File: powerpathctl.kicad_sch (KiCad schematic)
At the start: 10 parts, among them J10 Conn_01x06_Male, J11 Conn_01x06_Male_BAT_data, J8 Conn_01x03_Male_BAT_PWR_IN_NU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, J9 Conn_01x03_Male_BAT_PWR, Q1 SI7149ADP-T1-GE3, U7 LTC4412ES6

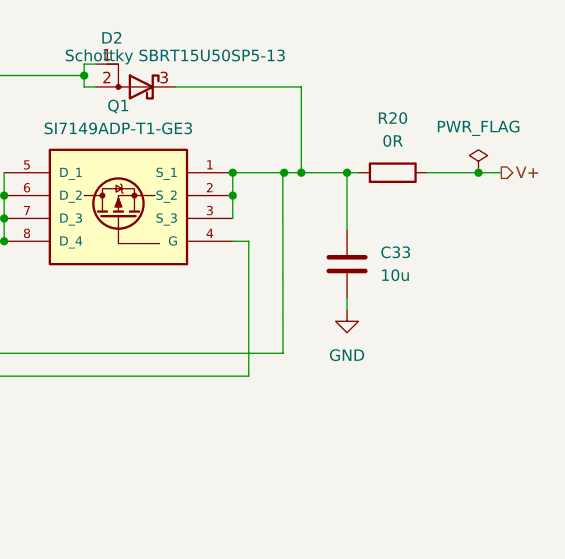
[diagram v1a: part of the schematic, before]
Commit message: optimized component selection, assigned missing LCSC part numbers
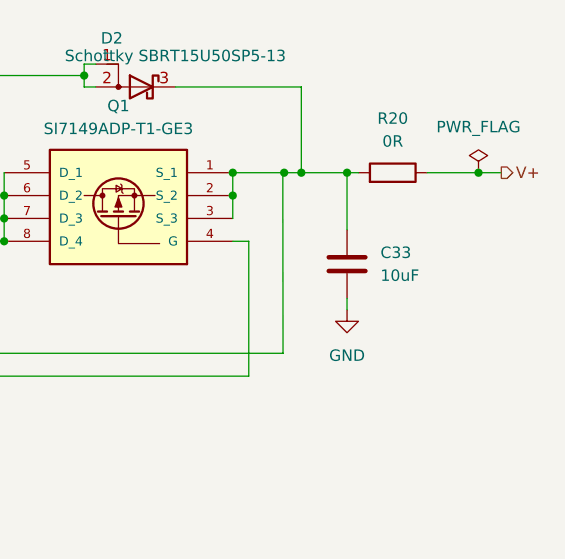
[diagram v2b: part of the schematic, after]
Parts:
- C33: value 10u -> 10uF
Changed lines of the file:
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@@
       (effects (font (size 1.27 1.27)) (justify left))
     )
-    (property "Value" "10u" (id 1) (at 192.9384 78.7399 0)
+    (property "Value" "10uF" (id 1) (at 192.9384 78.7399 0)
       (effects (font (size 1.27 1.27)) (justify left))
     )

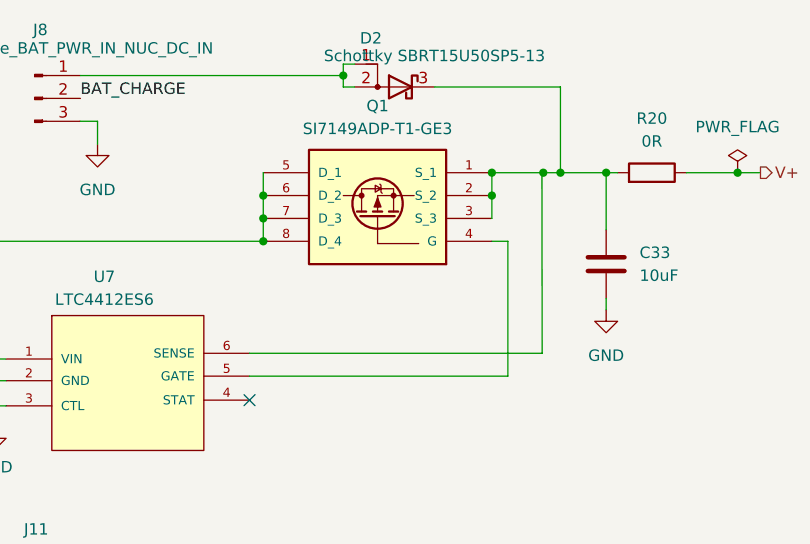
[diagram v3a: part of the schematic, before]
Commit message: motor connectors, optimized power path controller layout
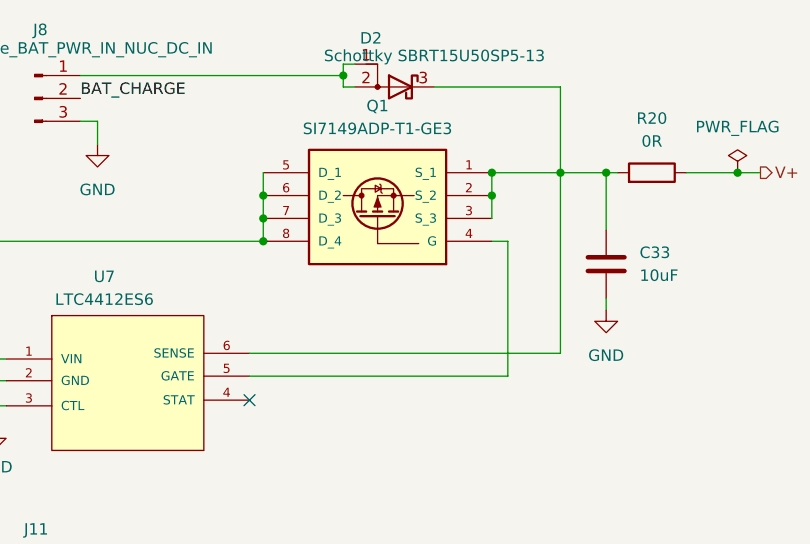
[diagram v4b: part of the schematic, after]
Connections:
- net at C33.1, D2.3 (K), R20.2: now also Q1.1 (S_1), Q1.2 (S_2), Q1.3 (S_3), U7.6 (SENSE)
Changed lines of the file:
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@@
   (junction (at 111.3028 120.269) (diameter 0) (color 0 0 0 0)
   )
-  (junction (at 184.15 67.31) (diameter 0) (color 0 0 0 0)
+  (junction (at 176.53 67.31) (diameter 0) (color 0 0 0 0)
   )
   (junction (at 151.13 69.85) (diameter 0) (color 0 0 0 0)
@@
   )
   (junction (at 121.285 74.93) (diameter 0) (color 0 0 0 0)
-  )
-  (junction (at 176.53 67.31) (diameter 0) (color 0 0 0 0)
   )
   (junction (at 151.13 74.93) (diameter 0) (color 0 0 0 0)
@@
   (junction (at 92.71 80.01) (diameter 0) (color 0 0 0 0)
   )
-  (junction (at 182.245 67.31) (diameter 0) (color 0 0 0 0)
+  (junction (at 151.13 72.39) (diameter 0) (color 0 0 0 0)
   )
-  (junction (at 151.13 72.39) (diameter 0) (color 0 0 0 0)
+  (junction (at 184.15 67.31) (diameter 0) (color 0 0 0 0)
   )
   (no_connect (at 149.606 92.583))
   (wire (pts (xy 132.715 61.595) (xy 132.715 64.135))
+    (stroke (width 0) (type default) (color 0 0 0 0))
+  )
+  (wire (pts (xy 176.53 67.31) (xy 184.15 67.31))
     (stroke (width 0) (type default) (color 0 0 0 0))
   )
@@
     (stroke (width 0) (type default) (color 0 0 0 0))
   )
+  (wire (pts (xy 184.15 87.376) (xy 184.15 67.31))
+    (stroke (width 0) (type default) (color 0 0 0 0))
+  )
   (wire (pts (xy 189.23 67.31) (xy 189.23 73.66))
     (stroke (width 0) (type default) (color 0 0 0 0))
@@
     (stroke (width 0) (type default) (color 0 0 0 0))
   )
+  (wire (pts (xy 149.606 87.376) (xy 184.15 87.376))
+    (stroke (width 0) (type default) (color 0 0 0 0))
+  )
   (wire (pts (xy 176.53 69.85) (xy 176.53 72.39))
     (stroke (width 0) (type default) (color 0 0 0 0))
   )
   (wire (pts (xy 108.6104 125.349) (xy 122.6312 125.349))
-    (stroke (width 0) (type default) (color 0 0 0 0))
-  )
-  (wire (pts (xy 182.245 67.31) (xy 184.15 67.31))
     (stroke (width 0) (type default) (color 0 0 0 0))
   )
@@
     (stroke (width 0) (type default) (color 0 0 0 0))
   )
-  (wire (pts (xy 149.606 87.376) (xy 182.118 87.376))
-    (stroke (width 0) (type default) (color 0 0 0 0))
-  )
   (wire (pts (xy 170.18 57.785) (xy 184.15 57.785))
     (stroke (width 0) (type default) (color 0 0 0 0))
   )
-  (wire (pts (xy 182.118 87.376) (xy 182.0926 67.31))
-    (stroke (width 0) (type default) (color 0 0 0 0))
-  )
-  (wire (pts (xy 176.53 67.31) (xy 182.0926 67.31))
-    (stroke (width 0) (type default) (color 0 0 0 0))
-  )

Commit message: more routing and pinout opt
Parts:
- removed R20, R21: 0R, Resistor_SMD:R_0603_1608Metric, symbol Device:R
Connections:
- net V+: now also C33.1, D2.3 (K), Q1.1 (S_1), Q1.2 (S_2), Q1.3 (S_3), U7.6 (SENSE)
- net VBAT+: now also Q1.5 (D_1), Q1.6 (D_2), Q1.7 (D_3), Q1.8 (D_4), U7.1 (VIN)
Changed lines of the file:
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@@
-    (stroke (width 0) (type default) (color 0 0 0 0))
-  )
-  (wire (pts (xy 120.015 74.93) (xy 121.285 74.93))
-    (stroke (width 0) (type default) (color 0 0 0 0))
-  )
-  (wire (pts (xy 198.12 67.31) (xy 203.835 67.31))
     (stroke (width 0) (type default) (color 0 0 0 0))
   )
@@
     (stroke (width 0) (type default) (color 0 0 0 0))
   )
-  (wire (pts (xy 103.505 74.93) (xy 112.395 74.93))
+  (wire (pts (xy 103.505 74.93) (xy 121.285 74.93))
     (stroke (width 0) (type default) (color 0 0 0 0))
   )
@@
     (stroke (width 0) (type default) (color 0 0 0 0))
   )
-  (wire (pts (xy 189.23 67.31) (xy 190.5 67.31))
+  (wire (pts (xy 189.23 67.31) (xy 203.835 67.31))
     (stroke (width 0) (type default) (color 0 0 0 0))
   )
@@
   (hierarchical_label "VBAT+" (shape output) (at 105.41 68.58 0)
     (effects (font (size 1.27 1.27)) (justify left))
-  )
-  (symbol (lib_id "Device:R") (at 194.31 67.31 270) (mirror x) (unit 1)
-    (in_bom yes) (on_board yes) (fields_autoplaced)
-    (property "Reference" "R20" (id 0) (at 194.31 61.2902 90))
-    (property "Value" "0R" (id 1) (at 194.31 63.8302 90))
-    (property "Footprint" "Resistor_SMD:R_0603_1608Metric" (id 2) (at 194.31 69.088 90)
-      (effects (font (size 1.27 1.27)) hide)
-    )
-    (property "Datasheet" "https://datasheet.lcsc.com/lcsc/2206010130_UNI-ROYAL-Uniroyal-Elec-0603WAF0000T5E_C21189.pdf" (id 3) (at 194.31 67.31 0)
-      (effects (font (size 1.27 1.27)) hide)
-    )
-    (property "LCSC" "C21189" (id 4) (at 194.31 67.31 90)
-      (effects (font (size 1.27 1.27)) hide)
-    )
-    (pin "1")
-    (pin "2")
   )
   (symbol (lib_id "Device:D_Schottky_AAK") (at 166.37 57.785 0) (mirror y) (unit 1)
@@
     (pin "1")
   )
-  (symbol (lib_id "Device:R") (at 116.205 74.93 270) (mirror x) (unit 1)
-    (in_bom yes) (on_board yes)
-    (property "Reference" "R21" (id 0) (at 115.9256 71.0692 90))
-    (property "Value" "0R" (id 1) (at 116.1288 72.644 90))
-    (property "Footprint" "Resistor_SMD:R_0603_1608Metric" (id 2) (at 116.205 76.708 90)
-      (effects (font (size 1.27 1.27)) hide)
-    )
-    (property "Datasheet" "https://datasheet.lcsc.com/lcsc/2206010130_UNI-ROYAL-Uniroyal-Elec-0603WAF0000T5E_C21189.pdf" (id 3) (at 116.205 74.93 0)
-      (effects (font (size 1.27 1.27)) hide)
-    )
-    (property "LCSC" "C21189" (id 4) (at 116.205 74.93 90)
-      (effects (font (size 1.27 1.27)) hide)
-    )
-    (pin "1")
-    (pin "2")
-  )
   (symbol (lib_id "LTC4412ES6:LTC4412ES6") (at 127.635 83.185 0) (unit 1)

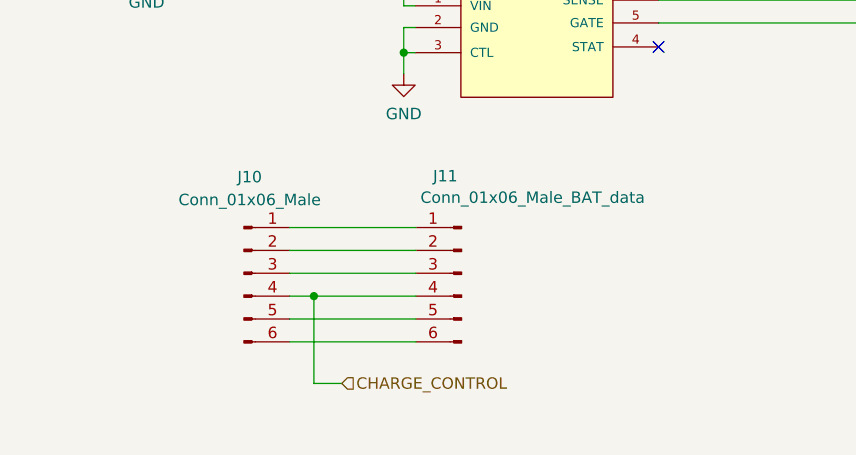
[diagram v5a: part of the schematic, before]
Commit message: first round of routing completed, led capacitors added to schematics
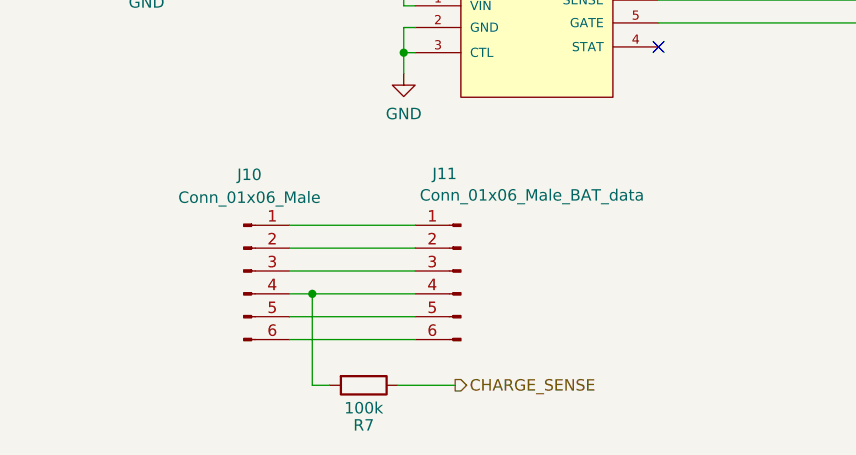
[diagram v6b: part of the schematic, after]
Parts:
- added R7: 100k, Resistor_SMD:R_0603_1608Metric, symbol Device:R
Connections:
- net CHARGE_CONTROL: no longer names the net of J10.4 (Pin_4), J11.4 (Pin_4)
- net CHARGE_CONTROL: now also R7.2
- new net CHARGE_SENSE: R7.1
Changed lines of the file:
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@@
   (junction (at 121.285 93.218) (diameter 0) (color 0 0 0 0)
   )
-  (junction (at 111.3028 120.269) (diameter 0) (color 0 0 0 0)
+  (junction (at 111.125 120.015) (diameter 0) (color 0 0 0 0)
   )
   (junction (at 176.53 67.31) (diameter 0) (color 0 0 0 0)
@@
     (stroke (width 0) (type default) (color 0 0 0 0))
   )
-  (wire (pts (xy 108.6104 117.729) (xy 122.6312 117.729))
-    (stroke (width 0) (type default) (color 0 0 0 0))
-  )
-  (wire (pts (xy 108.6104 115.189) (xy 122.6312 115.189))
+  (wire (pts (xy 108.585 117.475) (xy 122.555 117.475))
+    (stroke (width 0) (type default) (color 0 0 0 0))
+  )
+  (wire (pts (xy 108.585 114.935) (xy 122.555 114.935))
     (stroke (width 0) (type default) (color 0 0 0 0))
   )
@@
     (stroke (width 0) (type default) (color 0 0 0 0))
   )
-  (wire (pts (xy 108.6104 122.809) (xy 122.6312 122.809))
+  (wire (pts (xy 108.585 122.555) (xy 122.555 122.555))
     (stroke (width 0) (type default) (color 0 0 0 0))
   )
@@
     (stroke (width 0) (type default) (color 0 0 0 0))
   )
-  (wire (pts (xy 108.6104 120.269) (xy 111.3028 120.269))
+  (wire (pts (xy 108.585 120.015) (xy 111.125 120.015))
     (stroke (width 0) (type default) (color 0 0 0 0))
   )
@@
     (stroke (width 0) (type default) (color 0 0 0 0))
   )
-  (wire (pts (xy 111.3028 129.9718) (xy 114.4016 129.9718))
+  (wire (pts (xy 111.125 130.175) (xy 113.03 130.175))
     (stroke (width 0) (type default) (color 0 0 0 0))
   )
@@
     (stroke (width 0) (type default) (color 0 0 0 0))
   )
-  (wire (pts (xy 108.6104 125.349) (xy 122.6312 125.349))
+  (wire (pts (xy 108.585 125.095) (xy 122.555 125.095))
     (stroke (width 0) (type default) (color 0 0 0 0))
   )
@@
     (stroke (width 0) (type default) (color 0 0 0 0))
   )
+  (wire (pts (xy 120.65 130.175) (xy 127 130.175))
+    (stroke (width 0) (type default) (color 0 0 0 0))
+  )
   (wire (pts (xy 103.505 68.58) (xy 103.505 74.93))
     (stroke (width 0) (type default) (color 0 0 0 0))
@@
     (stroke (width 0) (type default) (color 0 0 0 0))
   )
-  (wire (pts (xy 111.3028 120.269) (xy 111.3028 129.9718))
+  (wire (pts (xy 111.125 120.015) (xy 111.125 130.175))
     (stroke (width 0) (type default) (color 0 0 0 0))
   )
@@
     (stroke (width 0) (type default) (color 0 0 0 0))
   )
-  (wire (pts (xy 108.6104 112.649) (xy 122.6312 112.649))
+  (wire (pts (xy 108.585 112.395) (xy 122.555 112.395))
     (stroke (width 0) (type default) (color 0 0 0 0))
   )
@@
     (stroke (width 0) (type default) (color 0 0 0 0))
   )
-  (wire (pts (xy 111.3028 120.269) (xy 122.6312 120.269))
+  (wire (pts (xy 111.125 120.015) (xy 122.555 120.015))
     (stroke (width 0) (type default) (color 0 0 0 0))
   )
@@
     (effects (font (size 1.27 1.27)) (justify left bottom))
   )
-  (hierarchical_label "CHARGE_CONTROL" (shape input) (at 114.4016 129.9718 0)
+  (hierarchical_label "CHARGE_SENSE" (shape output) (at 127 130.175 0)
     (effects (font (size 1.27 1.27)) (justify left))
   )
@@
     (pin "6")
   )
+  (symbol (lib_id "Device:R") (at 116.84 130.175 270) (unit 1)
+    (in_bom yes) (on_board yes)
+    (property "Reference" "R7" (id 0) (at 116.84 134.62 90))
+    (property "Value" "100k" (id 1) (at 116.84 132.715 90))
+    (property "Footprint" "Resistor_SMD:R_0603_1608Metric" (id 2) (at 116.84 128.397 90)
+      (effects (font (size 1.27 1.27)) hide)
+    )
+    (property "Datasheet" "https://datasheet.lcsc.com/lcsc/2206010045_UNI-ROYAL-Uniroyal-Elec-0603WAF1003T5E_C25803.pdf" (id 3) (at 116.84 130.175 0)
+      (effects (font (size 1.27 1.27)) hide)
+    )
+    (property "LCSC" "C25803" (id 4) (at 116.84 130.175 90)
+      (effects (font (size 1.27 1.27)) hide)
+    )
+    (pin "1")
+    (pin "2")
+  )
   (symbol (lib_id "Device:C") (at 189.23 77.47 0) (unit 1)
     (in_bom yes) (on_board yes) (fields_autoplaced)
@@
     (pin "1")
   )
-  (symbol (lib_id "Connector:Conn_01x06_Male") (at 127.7112 117.729 0) (mirror y) (unit 1)
-    (in_bom yes) (on_board yes)
-    (property "Reference" "J11" (id 0) (at 124.5362 106.934 0)
+  (symbol (lib_id "Connector:Conn_01x06_Male") (at 127.635 117.475 0) (mirror y) (unit 1)
+    (in_bom yes) (on_board yes)
+    (property "Reference" "J11" (id 0) (at 124.46 106.68 0)
       (effects (font (size 1.27 1.27)) (justify right))
     )
-    (property "Value" "Conn_01x06_Male_BAT_data" (id 1) (at 123.1392 109.3216 0)
+    (property "Value" "Conn_01x06_Male_BAT_data" (id 1) (at 123.063 109.0676 0)
       (effects (font (size 1.27 1.27)) (justify right))
     )
-    (property "Footprint" "Connector_JST:JST_PH_S6B-PH-K_1x06_P2.00mm_Horizontal" (id 2) (at 127.7112 117.729 0)
-      (effects (font (size 1.27 1.27)) hide)
-    )
-    (property "Datasheet" "~" (id 3) (at 127.7112 117.729 0)
+    (property "Footprint" "Connector_JST:JST_PH_S6B-PH-K_1x06_P2.00mm_Horizontal" (id 2) (at 127.635 117.475 0)
+      (effects (font (size 1.27 1.27)) hide)
+    )
+    (property "Datasheet" "~" (id 3) (at 127.635 117.475 0)
       (effects (font (size 1.27 1.27)) hide)
     )
@@
     (pin "1")
   )
-  (symbol (lib_id "Connector:Conn_01x06_Male") (at 103.5304 117.729 0) (unit 1)
-    (in_bom yes) (on_board yes) (fields_autoplaced)
-    (property "Reference" "J10" (id 0) (at 104.1654 107.0356 0))
-    (property "Value" "Conn_01x06_Male " (id 1) (at 104.1654 109.5756 0))
-    (property "Footprint" "Connector_JST:JST_PH_S6B-PH-K_1x06_P2.00mm_Horizontal" (id 2) (at 103.5304 117.729 0)
-      (effects (font (size 1.27 1.27)) hide)
-    )
-    (property "Datasheet" "~" (id 3) (at 104.4448 118.6942 0)
-      (effects (font (size 1.27 1.27)) hide)
-    )
+  (symbol (lib_id "Connector:Conn_01x06_Male") (at 103.505 117.475 0) (unit 1)
+    (in_bom yes) (on_board yes) (fields_autoplaced)
+    (property "Reference" "J10" (id 0) (at 104.14 106.7816 0))
+    (property "Value" "Conn_01x06_Male " (id 1) (at 104.14 109.3216 0))
+    (property "Footprint" "Connector_JST:JST_PH_S6B-PH-K_1x06_P2.00mm_Horizontal" (id 2) (at 103.505 117.475 0)
+      (effects (font (size 1.27 1.27)) hide)
+    )
+    (property "Datasheet" "~" (id 3) (at 104.4194 118.4402 0)
+      (effects (font (size 1.27 1.27)) hide)
+    )

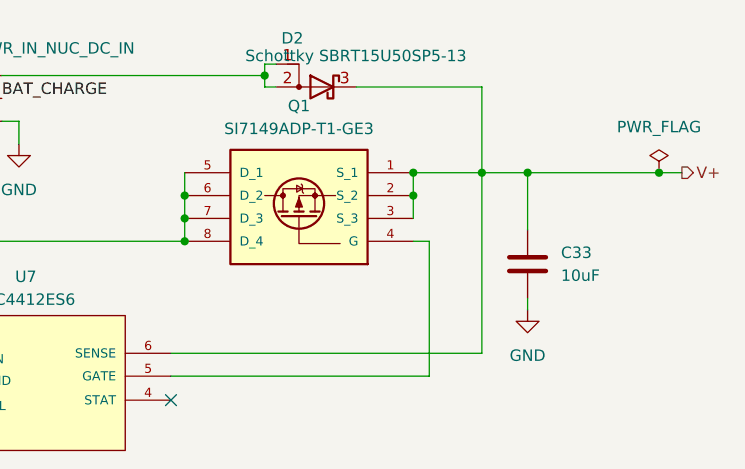
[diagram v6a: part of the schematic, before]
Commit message: led capacitors routed
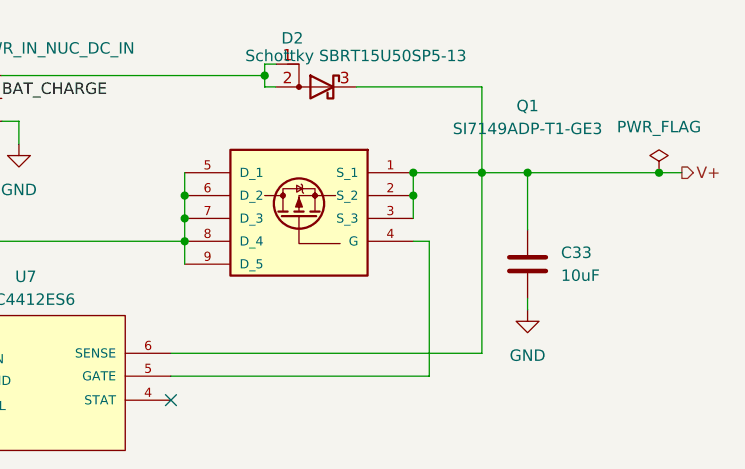
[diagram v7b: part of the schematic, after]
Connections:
- net VBAT+: now also Q1.9 (D_5)
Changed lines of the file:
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@@
+    (stroke (width 0) (type default) (color 0 0 0 0))
+  )
+  (wire (pts (xy 151.13 74.93) (xy 151.13 77.47))
     (stroke (width 0) (type default) (color 0 0 0 0))
   )
@@
   (symbol (lib_id "SI7149ADP-T1-GE3:SI7149ADP-T1-GE3") (at 176.53 67.31 0) (mirror y) (unit 1)
     (in_bom yes) (on_board yes) (fields_autoplaced)
-    (property "Reference" "Q1" (id 0) (at 163.83 59.8932 0))
-    (property "Value" "SI7149ADP-T1-GE3" (id 1) (at 163.83 62.4332 0))
+    (property "Reference" "Q1" (id 0) (at 189.23 59.8932 0))
+    (property "Value" "SI7149ADP-T1-GE3" (id 1) (at 189.23 62.4332 0))
     (property "Footprint" "Robotont:POWERPAKSO-8" (id 2) (at 176.53 67.31 0)
       (effects (font (size 1.27 1.27)) (justify bottom) hide)
@@
     (pin "7")
     (pin "8")
+    (pin "9")
   )
   (symbol (lib_id "power:GND") (at 189.23 82.55 0) (unit 1)
